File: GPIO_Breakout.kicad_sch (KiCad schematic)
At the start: 3 parts, among them J10 Port C/D breakout, J8 Port A breakout, J9 Port B breakout

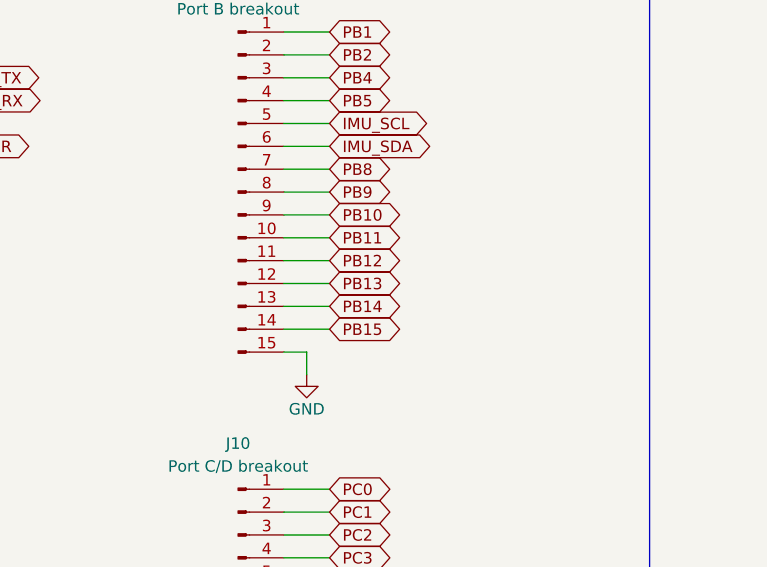
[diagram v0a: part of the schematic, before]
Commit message: Add power-rail and debug LEDs and an NRST pull-up
New Power_Indicators.kicad_sch sheet (page 8):
- One green LED per rail (Lite-On LTST-C190KGKT, 0603, 2.0 V typ):
  +12V D4/R17 4.7k, +5V 6A PI D5/R18 1.5k, +5V 6A AUX D6/R19 1.5k,
  +5V 2A D7/R20 1.5k, +3V3 D3/R3 510R (moved from the root sheet).
  About 2-2.7 mA each; worst-case resistor dissipation 34 mW (R17).
- Four yellow active-high STM32 debug LEDs (LTST-C190KSKT, 680R,
  1.8 mA): D8 LED_USER (PA5), D9 LED_PI_LINK (PB12), D10 LED_IMU
  (PB13), D11 LED_MOTOR (PB14). PB12-PB14 global labels are renamed
  at U1 and on the J9 breakout header.
- Uses the current KiCad Device:LED symbol, clearing the stale
  lib_symbol_mismatch warning on D3.

Add R25, a 10k 0805 pull-up from NRST to +3V3, alongside C13 and the
reset button, to keep the reset line firm against motor and
regulator noise.

Co-Authored-By: Claude Opus 5.5 <noreply@anthropic.com>
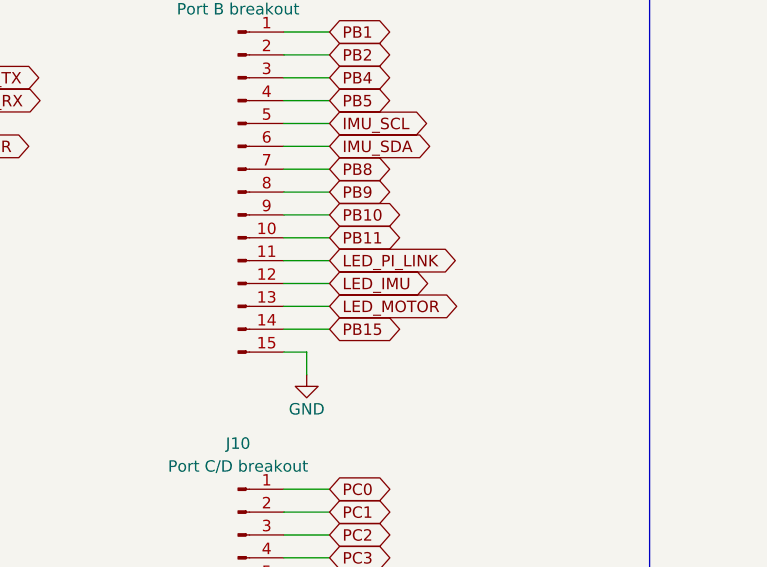
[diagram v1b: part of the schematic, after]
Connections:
- net PB12 renamed LED_PI_LINK
- net PB13 renamed LED_IMU
- net PB14 renamed LED_MOTOR
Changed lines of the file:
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@@
 		)
 	)
-	(global_label "PB14"
+	(global_label "LED_MOTOR"
 		(shape bidirectional)
 		(at 111.76 91.44 0)
@@
 		)
 	)
-	(global_label "PB13"
+	(global_label "LED_IMU"
 		(shape bidirectional)
 		(at 111.76 88.9 0)
@@
 		)
 	)
-	(global_label "PB12"
+	(global_label "LED_PI_LINK"
 		(shape bidirectional)
 		(at 111.76 86.36 0)
@@
 			)
 		)
-		(property "Description" "Male 2.54 mm pin header, 1x15 vertical: pins 1-14 = PB1, PB2, PB4, PB5, IMU_SCL (PB6), IMU_SDA (PB7), PB8, PB9, PB10, PB11, PB12, PB13, PB14, PB15; pin 15 = GND"
+		(property "Description" "Male 2.54 mm pin header, 1x15 vertical: pins 1-14 = PB1, PB2, PB4, PB5, IMU_SCL (PB6), IMU_SDA (PB7), PB8, PB9, PB10, PB11, LED_PI_LINK (PB12), LED_IMU (PB13), LED_MOTOR (PB14), PB15; pin 15 = GND"
 			(at 101.6 78.74 0)
 			(hide yes)
